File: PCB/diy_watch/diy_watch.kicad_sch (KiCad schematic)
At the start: 48 parts, among them IC1 W25Q16JVUXIQ, J1 USB_B_Micro, SW1 SW_Push, U1 FTE-2CA-V-T/R, U2 DS3231MZ, U3 RP2040, U7 XC6210B332MR, U8 LTC4071EMS8E_PBF, Y1 12MHz_crystal

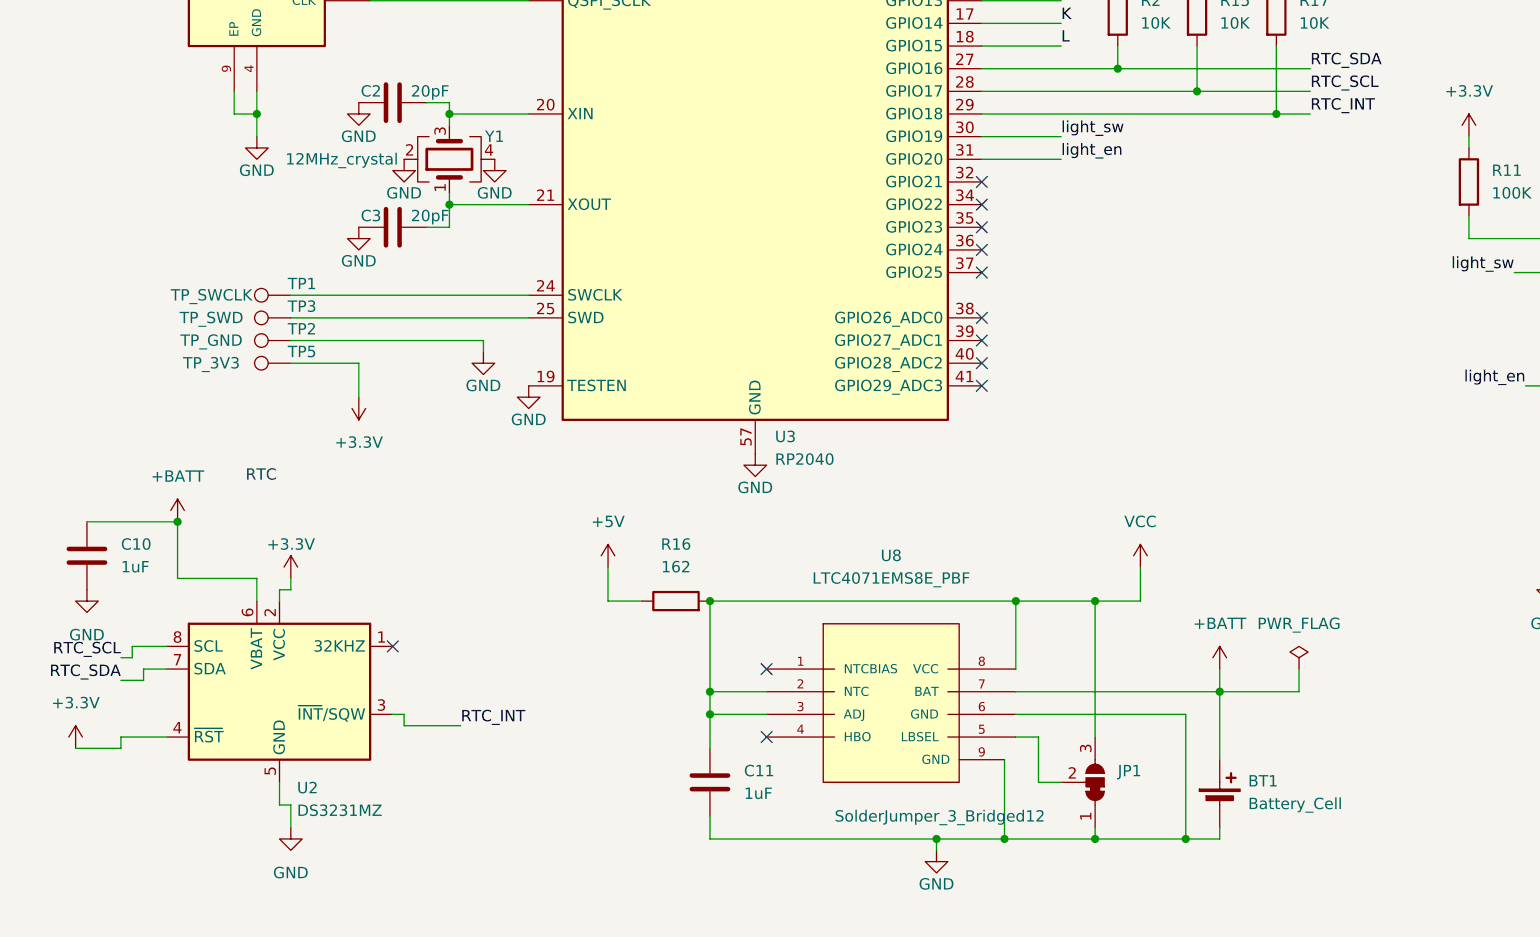
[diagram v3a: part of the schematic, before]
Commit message: Updating PCB with new RTC, charger, smaller ocillators
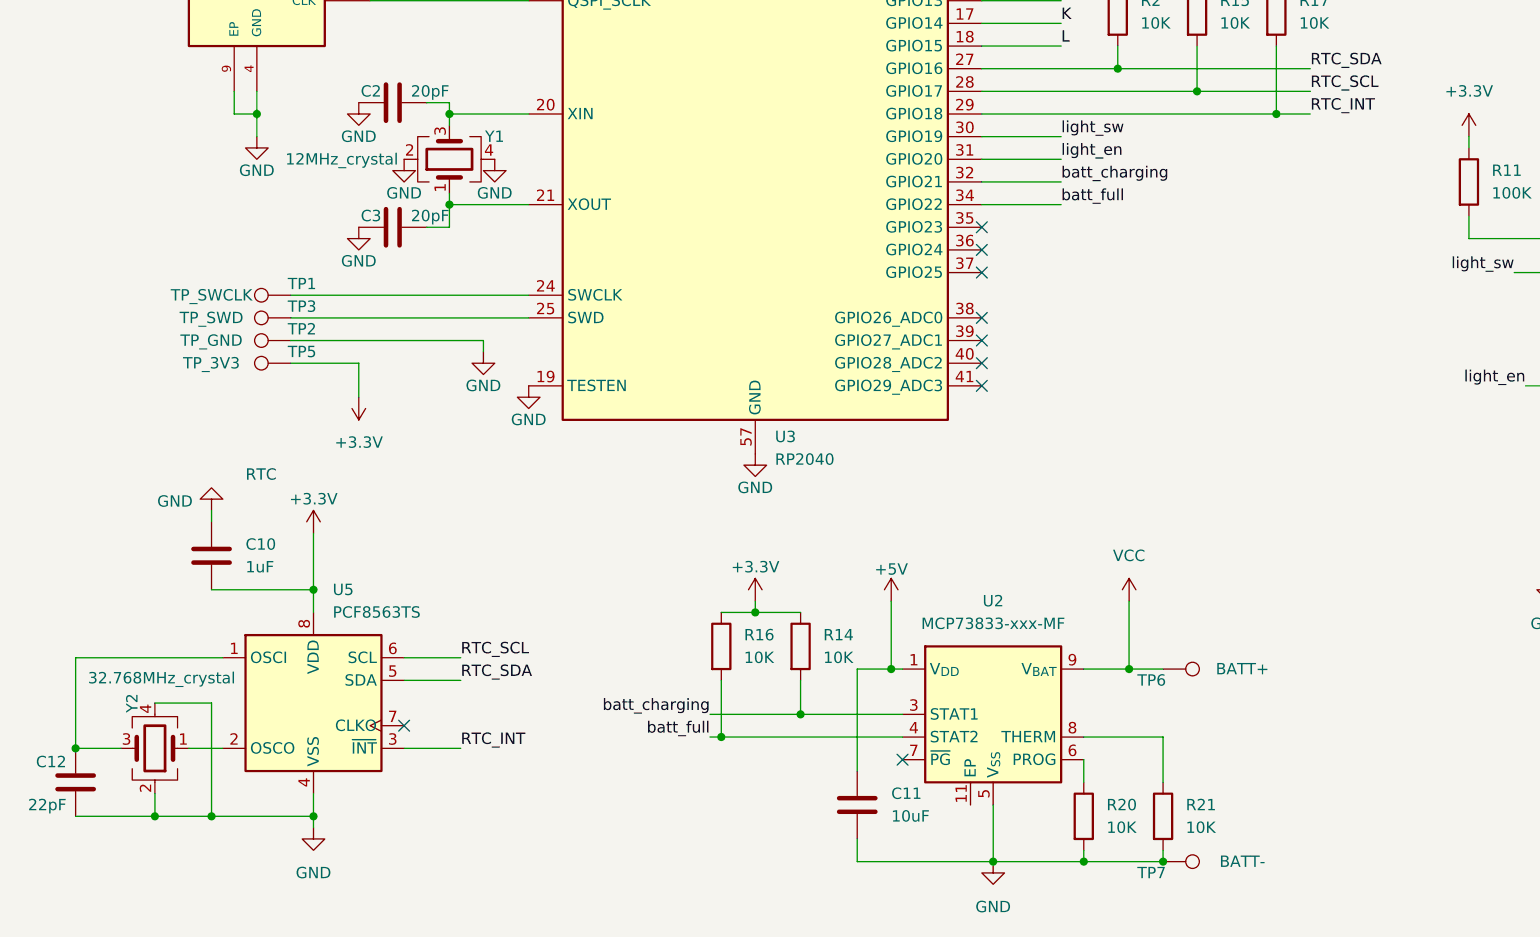
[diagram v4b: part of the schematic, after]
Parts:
- removed BT1: Battery_Cell, Battery:BatteryHolder_Multicomp_BC-2001_1x2032, symbol Device:Battery_Cell
- removed JP1: SolderJumper_3_Bridged12, Jumper:SolderJumper-3_P1.3mm_Bridged12_RoundedPad1.0x1.5mm, symbol Jumper:SolderJumper_3_Bridged12
- removed U2: DS3231MZ, Package_SO:SOIC-8_3.9x4.9mm_P1.27mm, symbol Timer_RTC:DS3231MZ
- removed U8: LTC4071EMS8E_PBF, Package_SO:MSOP-8-1EP_3x3mm_P0.65mm_EP1.95x2.15mm, symbol DIY_Watch_lib:LTC4071EMS8E_PBF
- added C12: 22pF, Capacitor_SMD:C_0402_1005Metric, symbol Device:C
- added R14, R20, R21: 10K, Resistor_SMD:R_0402_1005Metric, symbol Device:R
- added TP6: BATT+, TestPoint:TestPoint_Pad_D1.5mm, symbol Connector:TestPoint
- added TP7: BATT-, TestPoint:TestPoint_Pad_D1.5mm, symbol Connector:TestPoint
- added U2: MCP73833-xxx-MF, Package_DFN_QFN:DFN-10-1EP_3x3mm_P0.5mm_EP1.58x2.35mm, symbol Battery_Management:MCP73833-xxx-MF
- added U5: PCF8563TS, Package_SO:MSOP-8_3x3mm_P0.65mm, symbol Timer_RTC:PCF8563TS
- added Y2: 32.768MHz_crystal, Crystal:Crystal_SMD_2520-4Pin_2.5x2.0mm, symbol Device:Crystal_GND24
- C11: value 1uF -> 10uF; JLCPCB Part C52923 -> (none)
- R16: value 162 -> 10K; JLCPCB Part C25091 -> C25744
- Y1: footprint Crystal:Crystal_SMD_3225-4Pin_3.2x2.5mm -> Crystal:Crystal_SMD_2520-4Pin_2.5x2.0mm; JLCPCB Part C9002 -> C252259
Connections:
- net +BATT is gone; now on net GND: C10.1
- net +3.3V: now also C10.2, R16.1, R14.1, U5.8 (VDD)
- net +5V: now also C11.1, U2.1 (V_{DD}), U2.2 (V_{DD}); no longer R16.1
- net GND: now also C12.1, R20.2, R21.2, TP7.1, U2.5 (V_{SS}), U5.4 (VSS), Y2.2, Y2.4; no longer C10.2
- net RTC_INT: now also U5.3 (~{INT})
- net RTC_SCL: now also U5.6 (SCL)
- net RTC_SDA: now also U5.5 (SDA)
- net VCC: now also TP6.1, U2.10 (V_{BAT}), U2.9 (V_{BAT}); no longer C11.1, R16.2
- net batt_charging: now reaches U3.32 (GPIO21)
- net batt_charging: now also R14.2, U2.3 (STAT1)
- net batt_full: now reaches U3.34 (GPIO22)
- net batt_full: now also R16.2, U2.4 (STAT2)
- new net: U5.2 (OSCO), Y2.1
- new net: C12.2, U5.1 (OSCI), Y2.3
- new net: R21.1, U2.8 (THERM)
- new net: R20.1, U2.6 (PROG)
- no-connect marks 15 -> 12
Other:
- moved on the sheet: C10
